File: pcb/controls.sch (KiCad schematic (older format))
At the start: 27 parts, among them J6 Conn_01x16, J7 Conn_01x06

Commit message: Version 2 PCB design (WIP)
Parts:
- J4: renamed from J6; footprint local:Amphenol_T821116A1S100CEU -> Local:Amphenol_T821116A1S100CEU
- J5: renamed from J7; footprint local:Amphenol_T821106A1S100CEU -> Local:Amphenol_T821106A1S100CEU
- RV2: footprint local:Citec_CB10LV103M -> Local:Citec_CB10LV103M
- renumbered R41 to R38, R40 to R39, R39 to R40, R42 to R41, R43 to R42, R44 to R43, R45 to R44, R38 to R45, TP50 to TP49, TP51 to TP50, TP52 to TP51, TP53 to TP52, TP54 to TP53, TP55 to TP54, TP56 to TP55, TP57 to TP56, TP62 to TP57, TP63 to TP58, TP58 to TP59, TP59 to TP60, TP60 to TP61, TP61 to TP62
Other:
- note added: "CONFIRM_n_RAW is usually held\nhigh by R41. When the button is\npressed, CONFIRM_n_RAW is\npulled to 0V. R43 and C14 form\na debouncing filter.\n\nLikewise for the CANCEL button."
- note removed: "CONFIRM_n_RAW is usually held\nhigh by R42. When button is\npressed, CONFIRM_n_RAW is\npulled to 0V. R44 and C14 form\na debouncing filter.\n\nLikewise for the CANCEL button."

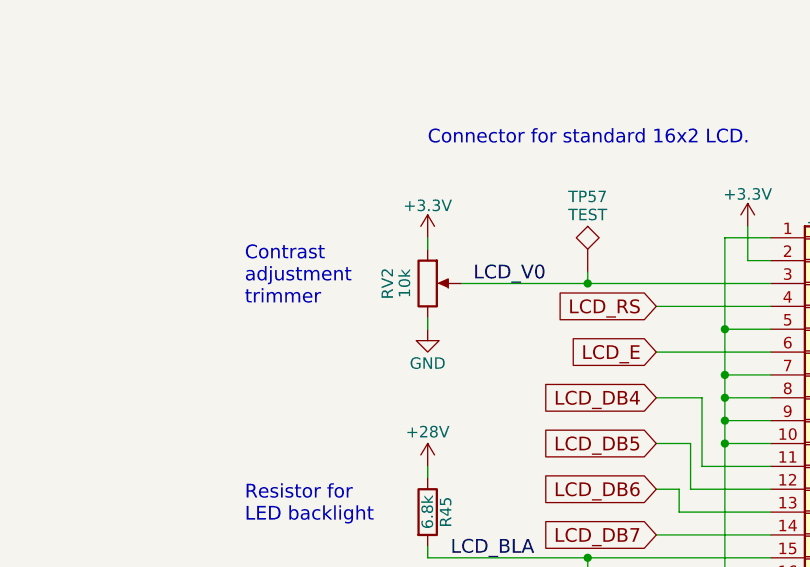
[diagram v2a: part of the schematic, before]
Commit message: pcb: change RV1, RV2 and R10 to be 22k instead of 10k
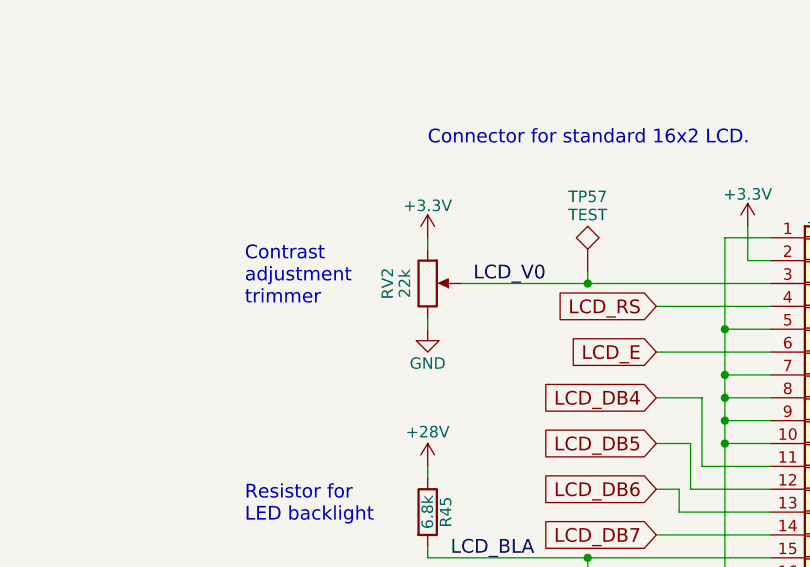
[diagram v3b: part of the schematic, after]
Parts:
- RV2: value 10k -> 22k
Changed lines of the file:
@@
 P 7900 4050
 F 0 "RV2" V 7725 4050 50  0000 C CNN
-F 1 "10k" V 7800 4050 50  0000 C CNN
+F 1 "22k" V 7800 4050 50  0000 C CNN
 F 2 "Local:Citec_CB10LV103M" H 7900 4050 50  0001 C CNN
 F 3 "" H 7900 4050 50  0001 C CNN
